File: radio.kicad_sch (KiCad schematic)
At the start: 3 parts, among them U2 SX1278

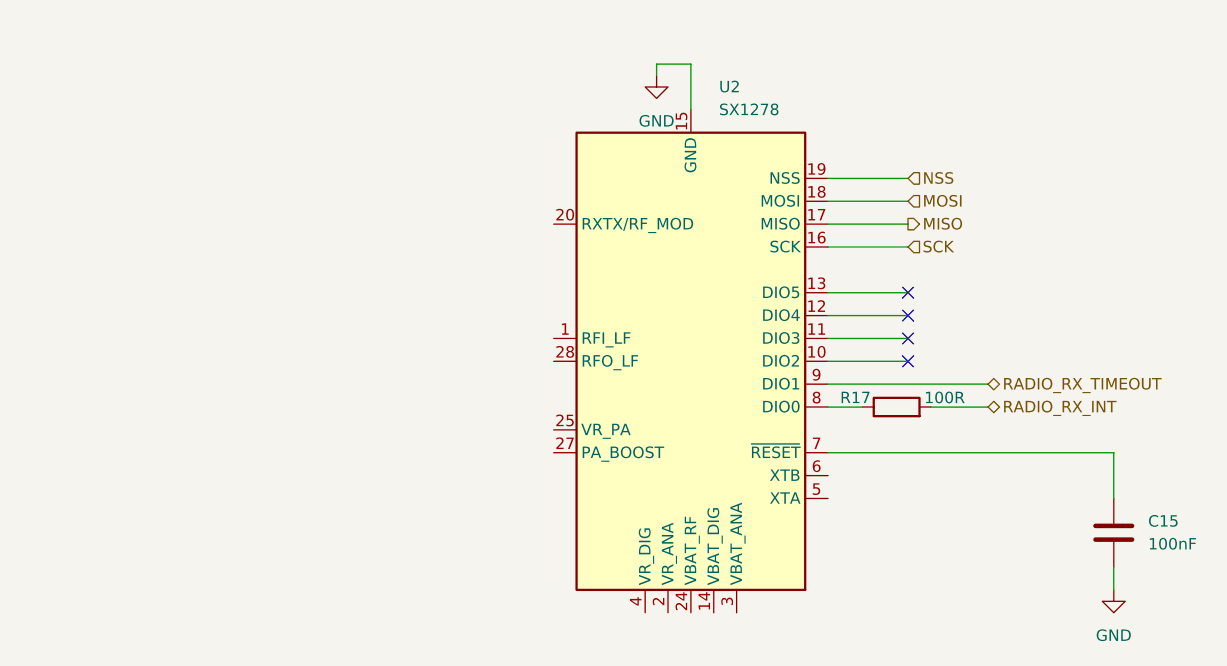
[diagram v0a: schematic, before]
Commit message: Add new LoRa module
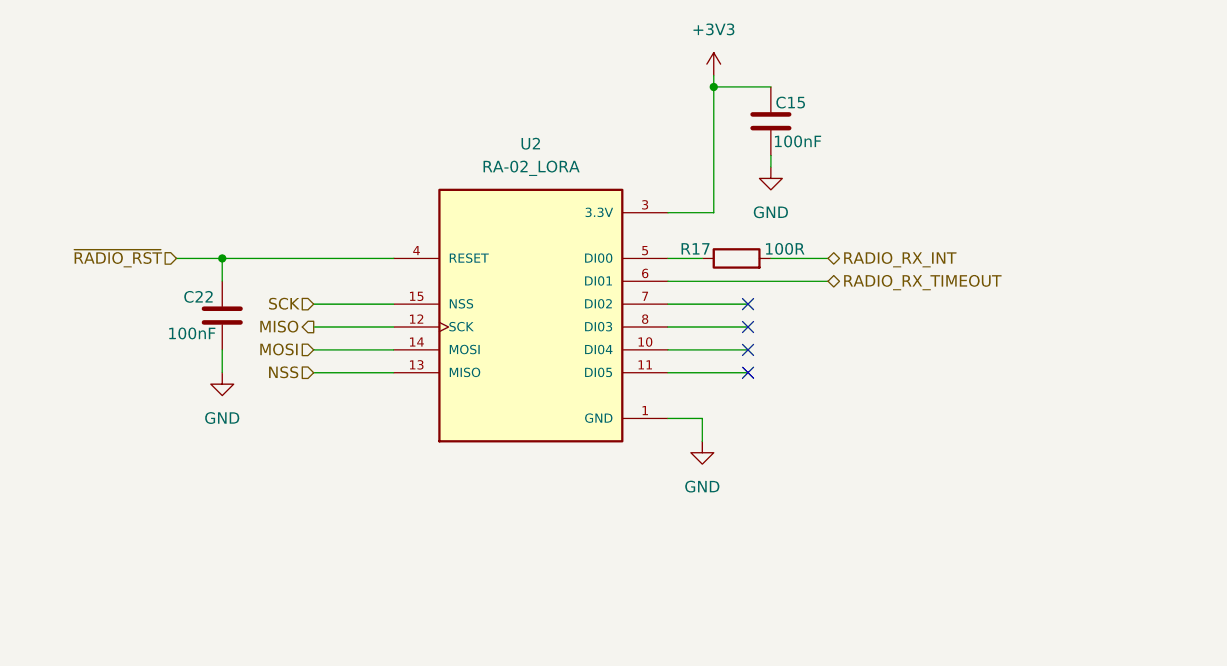
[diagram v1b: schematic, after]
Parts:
- removed U2: SX1278, Package_DFN_QFN:QFN-28-1EP_6x6mm_P0.65mm_EP4.8x4.8mm, symbol RF:SX1278
- added C22: 100nF, symbol Device:C
- added U2: RA-02_LORA, RA-02_LORA:MODULE_RA-02_LORA, symbol RA-02_LORA:RA-02_LORA
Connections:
- net GND: now also C22.2, U2.1 (GND), U2.16 (GND), U2.2 (GND), U2.9 (GND)
- net MISO: now also U2.12 (SCK)
- net MOSI: now also U2.14 (MOSI)
- net NSS: now also U2.13 (MISO)
- net RADIO_RX_TIMEOUT: now also U2.6 (DI01)
- net SCK: now also U2.15 (NSS)
- net +3V3: now reaches C15.1
- net +3V3: now also U2.3 (3.3V)
- net at R17.1: now also U2.5 (DI00)
- new net ~{RADIO_RST}: C22.1, U2.4 (RESET)
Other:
- moved on the sheet: R17

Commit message: Assigned footprints and drew pcb outline
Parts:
- C15, C22: footprint (none) -> Capacitor_Tantalum_SMD:CP_EIA-2012-15_AVX-P
- R17: footprint (none) -> Resistor_SMD:R_0805_2012Metric
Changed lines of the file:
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@@
 			)
 		)
-		(property "Footprint" ""
+		(property "Footprint" "Resistor_SMD:R_0805_2012Metric"
 			(at 148.59 89.408 90)
 			(effects
@@
 			)
 		)
-		(property "Footprint" ""
+		(property "Footprint" "Capacitor_Tantalum_SMD:CP_EIA-2012-15_AVX-P"
 			(at 153.3652 76.2 0)
 			(effects
@@
 			)
 		)
-		(property "Footprint" ""
+		(property "Footprint" "Capacitor_Tantalum_SMD:CP_EIA-2012-15_AVX-P"
 			(at 92.4052 97.79 0)
 			(effects

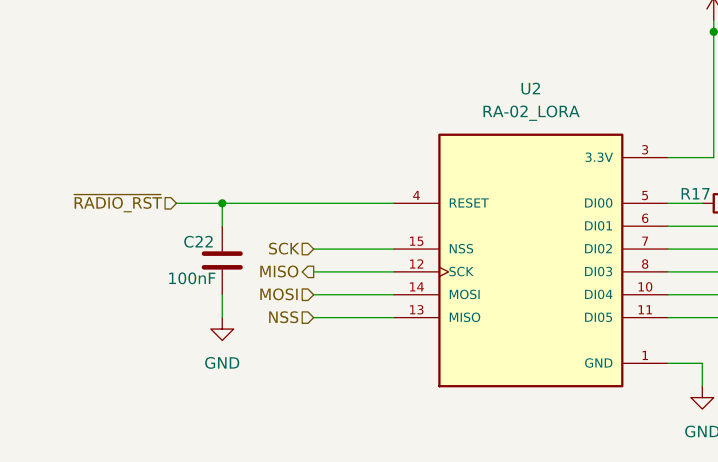
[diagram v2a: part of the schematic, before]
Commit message: Changed LoRa module to RFM98W 433MHz
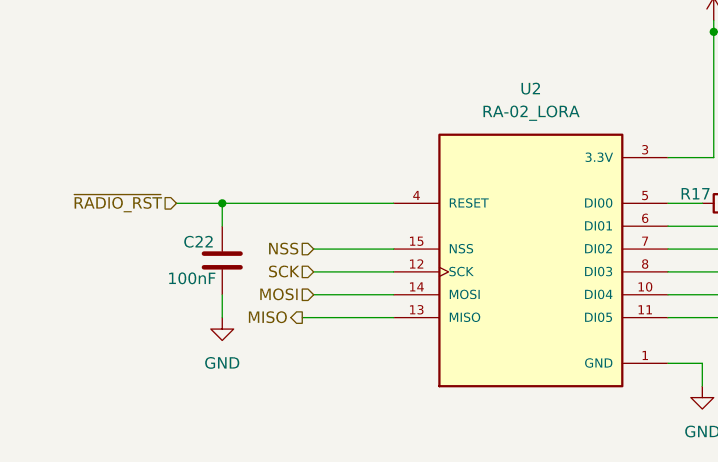
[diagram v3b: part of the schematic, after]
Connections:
- net MISO: now also U2.13 (MISO); no longer U2.12 (SCK)
- net NSS: now also U2.15 (NSS); no longer U2.13 (MISO)
- net SCK: now also U2.12 (SCK); no longer U2.15 (NSS)
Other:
- company: (none) -> Team ApolLO
- title: (none) -> Radio
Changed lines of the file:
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@@
 	(generator_version "9.0")
 	(paper "A4")
+	(title_block
+		(title "Radio")
+		(date "2026-01-17")
+		(rev "1.0.1")
+		(company "Team ApolLO")
+		(comment 1 "Author: Wiktor Kociuba")
+	)
 	(junction
 		(at 146.05 68.58)
@@
 	(wire
 		(pts
-			(xy 110.49 100.33) (xy 101.6 100.33)
+			(xy 110.49 100.33) (xy 100.33 100.33)
 		)
 		(stroke
@@
 		)
 	)
-	(hierarchical_label "SCK"
-		(shape input)
-		(at 101.6 92.71 180)
-		(effects
-			(font
-				(size 1.27 1.27)
-			)
-			(justify right)
-		)
-	)
 	(hierarchical_label "~{RADIO_RST}"
 		(shape input)
 		(at 86.36 87.63 180)
-		(effects
-			(font
-				(size 1.27 1.27)
-			)
-			(justify right)
-		)
-	)
-	(hierarchical_label "MISO"
-		(shape output)
-		(at 101.6 95.25 180)
 		(effects
 			(font
@@
 		)
 	)
+	(hierarchical_label "SCK"
+		(shape input)
+		(at 101.6 95.25 180)
+		(effects
+			(font
+				(size 1.27 1.27)
+			)
+			(justify right)
+		)
+	)
+	(hierarchical_label "MISO"
+		(shape output)
+		(at 100.33 100.33 180)
+		(effects
+			(font
+				(size 1.27 1.27)
+			)
+			(justify right)
+		)
+	)
 	(hierarchical_label "RADIO_RX_INT"
 		(shape bidirectional)
@@
 	(hierarchical_label "NSS"
 		(shape input)
-		(at 101.6 100.33 180)
-		(effects
-			(font
+		(at 101.6 92.71 180)
+		(effects
+			(font
